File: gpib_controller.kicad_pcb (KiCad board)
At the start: 4 copper layers, 58.6 x 64.6 mm, 43 parts, among them J1 112-024-113R001, J2 FTSH-105-01-L-DV-K, J3 RJHSE5380, J4 USB4085-GF-A, U1 SN74LVC8T245PWR, U2 SN74LVC07APWR, U3 STM32H533RETx, U4 PTS645SH43SMTR92 LFS, U5 THVD1451D, U6 SN74LVC1G07DCKR, U7 SN74LVC14APWR, U8 USBLC6-2SC6, U9 TPSM861253RDXR, Y1 MU00525-32.768K, Y2 CS10820-24M

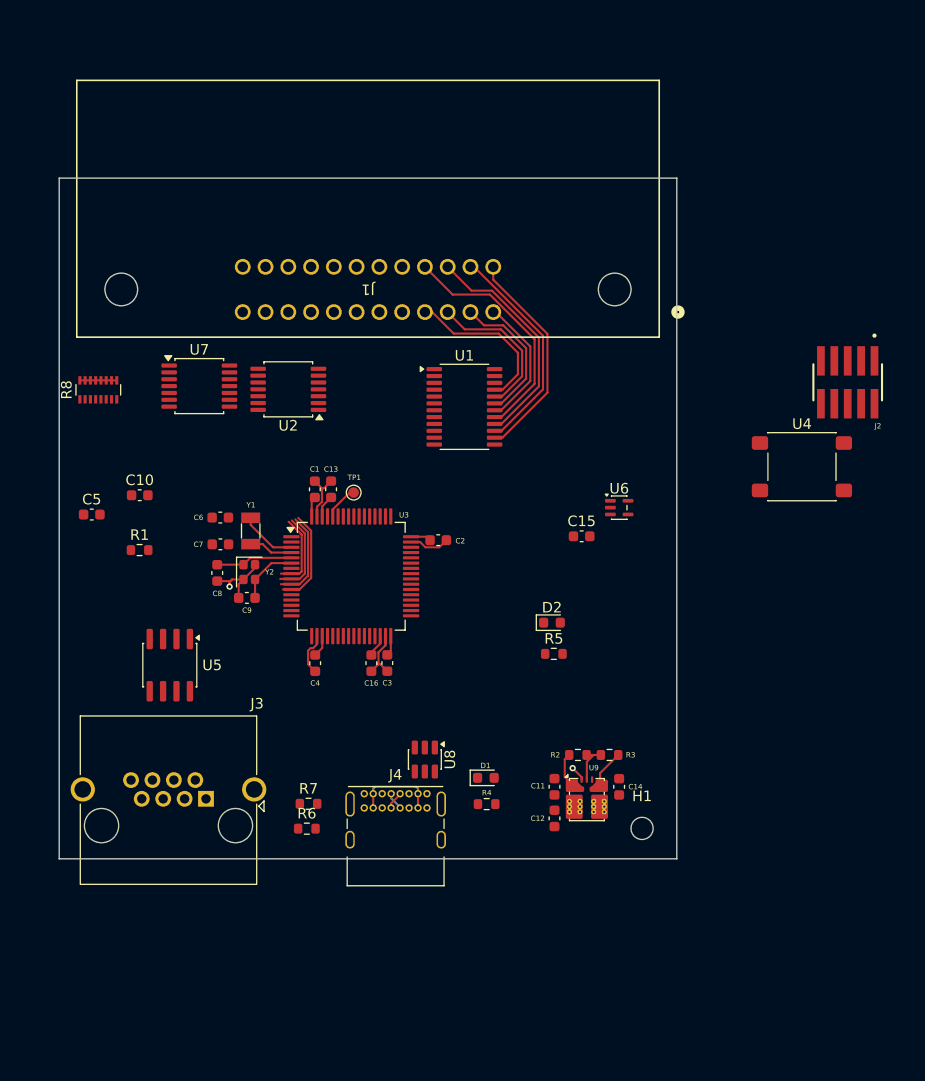
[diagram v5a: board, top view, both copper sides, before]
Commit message: Change board size, complete bottom routing, update (still broken) jobfile
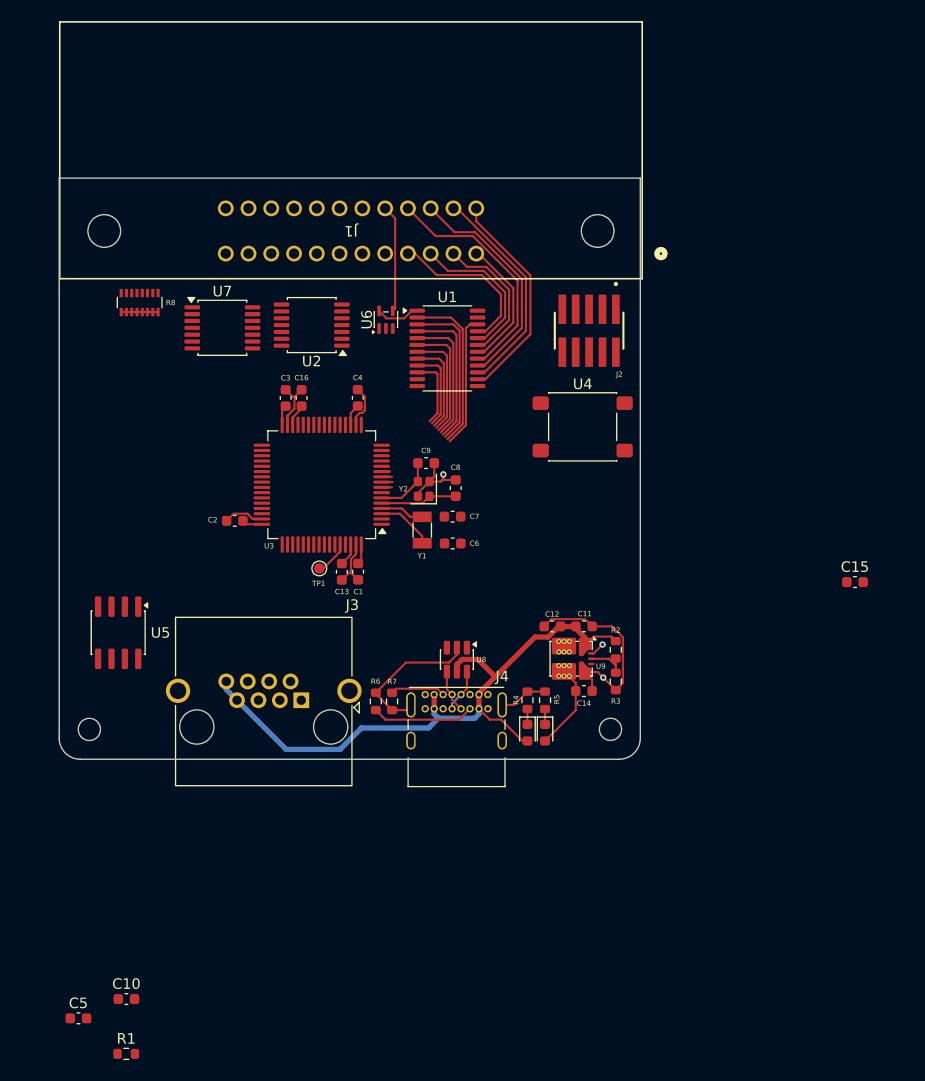
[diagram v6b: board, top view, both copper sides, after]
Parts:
- added H2: MountingHole, MountingHole:MountingHole_2.1mm, F.Cu at (189.4, 120.9)
- moved H1 53.3 mm to (140.0, 120.9)
- moved R1 47.8 mm to (143.4, 151.7)
- moved C5 47.8 mm to (138.9, 148.3)
- moved C10 47.8 mm to (143.5, 146.4)
- moved U6 28.4 mm to (168.1, 82.0), turned to 90 degrees
- moved C3 26.9 mm to (158.6, 89.4), turned to 90 degrees
- moved C15 26.3 mm to (212.6, 106.9)
- moved C16 26.0 mm to (160.1, 89.4), turned to 90 degrees
- moved C4 25.5 mm to (165.4, 89.4), turned to 90 degrees
- moved J2 25.0 mm to (187.3, 83.1)
- moved C8 24.0 mm to (174.7, 98.0), turned to -90 degrees
- moved C6 22.2 mm to (174.4, 103.2), turned to 180 degrees
- moved C7 22.2 mm to (174.4, 100.7), turned to 180 degrees
- moved C9 21.3 mm to (171.9, 95.6), turned to 180 degrees
- moved U4 21.1 mm to (186.7, 92.2)
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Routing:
- net +5V: track 15.0 -> 64.7 mm
- net GND: track 28.7 -> 63.3 mm, vias 1 -> 2
- net /Overview/GPIB Transceiver/GPIB_DIR: track 0.00 -> 15.8 mm
- net /Overview/GPIB Transceiver/GPIB_EN: track 0.00 -> 12.6 mm
- net +3V3: track 9.28 -> 21.8 mm
- net /Overview/GPIB Transceiver/iDIO8: track 0.00 -> 10.3 mm
- net /Overview/Connectors/REN: track 0.00 -> 10.2 mm
- net Net-(J4-CC2): track 0.00 -> 9.74 mm
- net /Overview/GPIB Transceiver/iDIO7: track 0.00 -> 9.02 mm
- net /Overview/GPIB Transceiver/iDIO6: track 0.00 -> 7.93 mm
- net /Overview/GPIB Transceiver/iDIO5: track 0.00 -> 6.79 mm
- net /Overview/GPIB Transceiver/iDIO4: track 9.33 -> 15.7 mm
- net /Overview/GPIB Transceiver/iDIO3: track 8.76 -> 14.9 mm
- net /Overview/GPIB Transceiver/iDIO2: track 8.11 -> 13.7 mm
- net Net-(J4-CC1): track 0.00 -> 5.23 mm
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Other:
- board size 58.6 x 64.6 mm -> 55.1 x 55.1 mm
- board text added: "3V3"
- board text added: "5V"

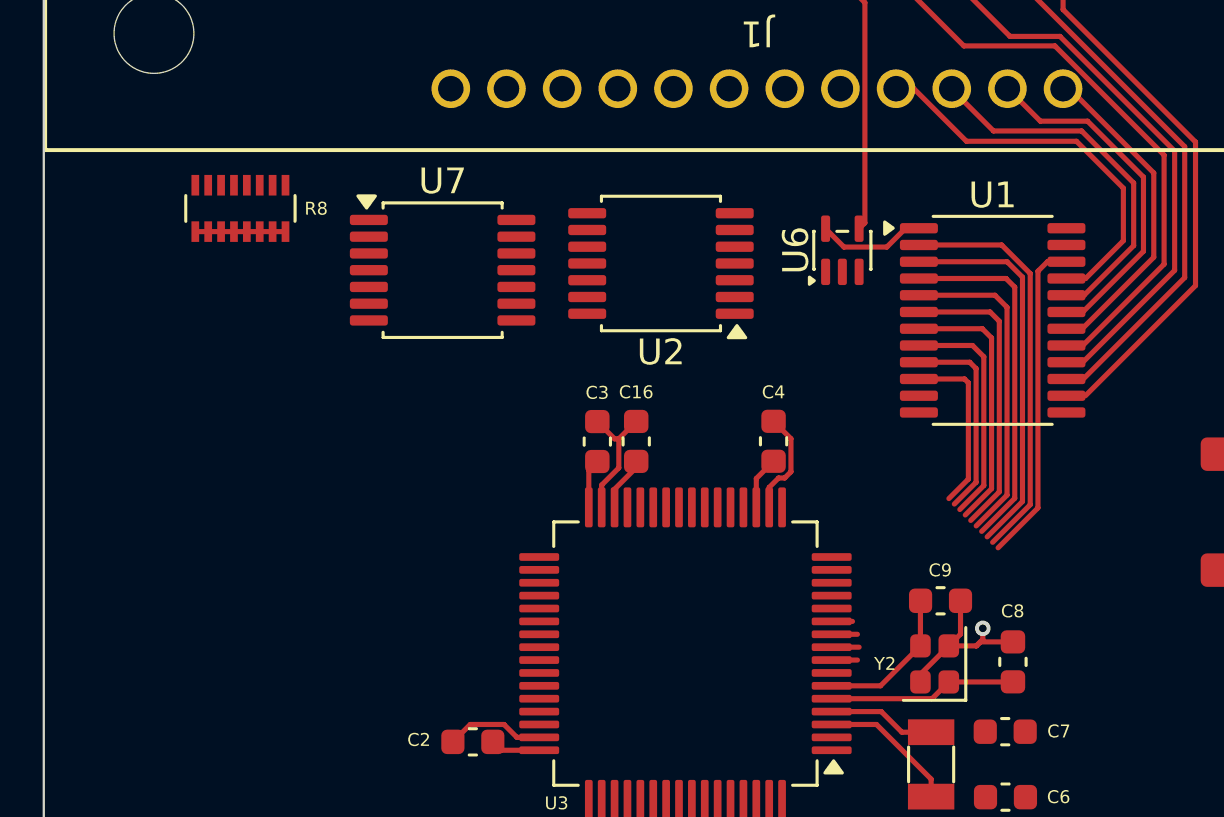
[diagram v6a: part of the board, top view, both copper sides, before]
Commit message: Update microcontroller pinouts and finished routing of DIO1-4
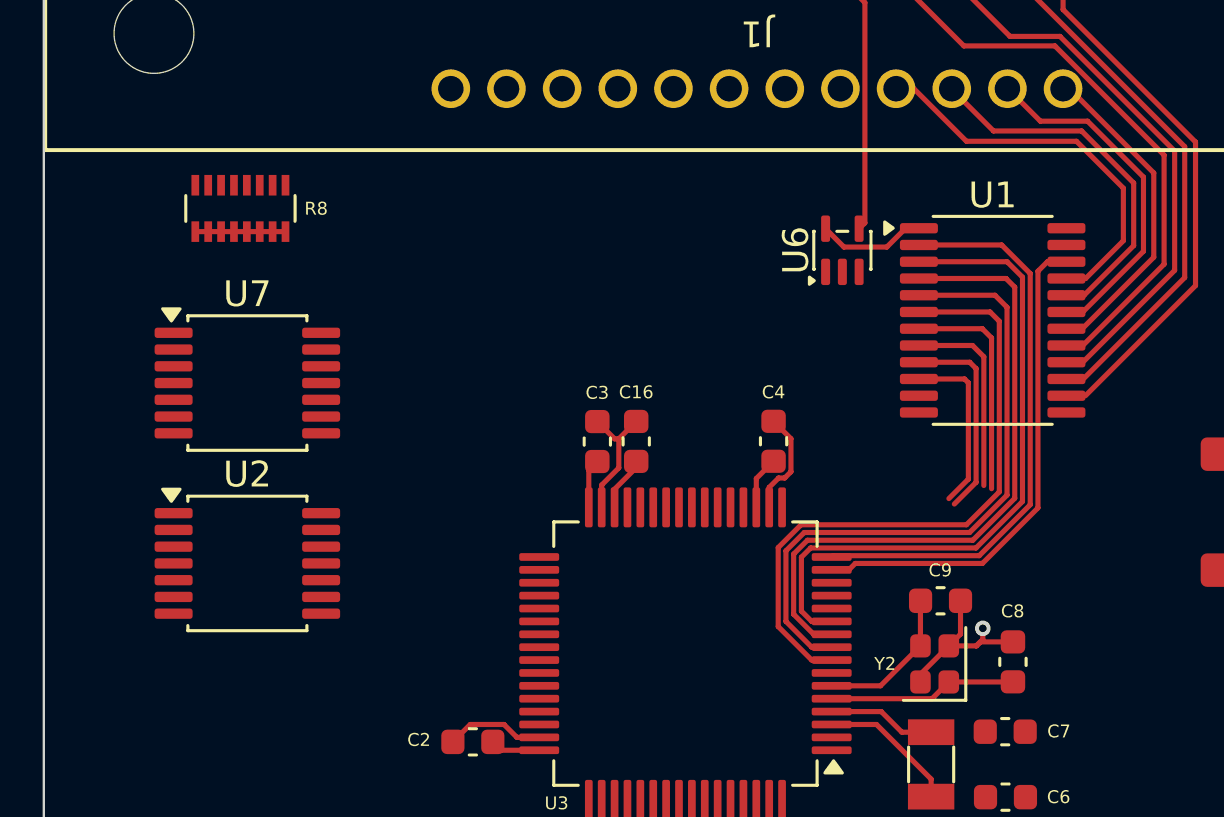
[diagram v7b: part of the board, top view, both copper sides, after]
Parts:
- moved U2 19.8 mm to (145.0, 94.2), turned to 0 degrees
- moved U7 8.75 mm to (145.0, 87.2)
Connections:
- U3 pad 15: /Overview/GPIB Transceiver/iDAV -> /Overview/GPIB Transceiver/GPIB_EN
- U3 pad 16: unconnected-(U3E-PA2(USART2_TX)-Pad16) -> /Overview/GPIB Transceiver/GPIB_DIR
- U3 pad 27: unconnected-(U3H-PB1-Pad27) -> /Overview/GPIB Transceiver/iDAV
- U3 pad 39: /Overview/GPIB Transceiver/GPIB_EN -> unconnected-(U3H-PC8-Pad39)
- U3 pad 40: /Overview/GPIB Transceiver/GPIB_DIR -> unconnected-(U3H-PC9-Pad40)
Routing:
- net /Overview/GPIB Transceiver/iDIO1: track 12.5 -> 25.0 mm
- net /Overview/GPIB Transceiver/iDIO2: track 13.7 -> 25.3 mm
- net /Overview/GPIB Transceiver/iDIO3: track 14.9 -> 25.7 mm
- net /Overview/GPIB Transceiver/iDIO4: track 15.7 -> 25.9 mm
- net /Overview/GPIB Transceiver/GPIB_EN: track 12.6 -> 19.4 mm
- net /Overview/GPIB Transceiver/GPIB_DIR: track 15.8 -> 22.3 mm
- net /Overview/GPIB Transceiver/iDIO8: track 10.3 -> 8.82 mm
- net /Overview/GPIB Transceiver/iDIO7: track 9.02 -> 7.70 mm

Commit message: Routing progress
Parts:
- moved C5 50.8 mm to (167.0, 105.9), turned to -90 degrees
- moved R1 47.1 mm to (161.7, 108.2)
- moved U4 44.3 mm to (143.6, 102.3), turned to -90 degrees
- moved J2 41.3 mm to (152.7, 105.7)
- moved C10 41.1 mm to (148.5, 105.7), turned to 90 degrees
- moved C15 23.1 mm to (190.7, 114.4), turned to 90 degrees
- moved U2 19.4 mm to (160.9, 83.0)
- moved U7 7.87 mm to (151.7, 83.0)
- moved C16 1.28 mm to (158.8, 89.4)
- moved C3 1.28 mm to (157.3, 89.4)
- moved U5 1.25 mm to (143.5, 112.7)
- moved C11 0.69 mm to (186.2, 111.0)
- moved C12 0.69 mm to (183.2, 111.0)
- moved C14 0.69 mm to (186.2, 117.2)
- moved R2 0.69 mm to (189.2, 113.3)
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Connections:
- R8 pad 1: /Overview/Connectors/DAV -> /Overview/Connectors/ATN
- R8 pad 2: /Overview/Connectors/NRFD -> /Overview/Connectors/SRQ
- R8 pad 3: /Overview/Connectors/NDAC -> /Overview/Connectors/IFC
- R8 pad 4: /Overview/Connectors/ATN -> /Overview/Connectors/NDAC
- R8 pad 5: /Overview/Connectors/IFC -> /Overview/Connectors/NRFD
- R8 pad 6: /Overview/Connectors/EOI -> /Overview/Connectors/DAV
- R8 pad 7: /Overview/Connectors/REN -> /Overview/Connectors/EOI
- R8 pad 8: /Overview/Connectors/SRQ -> /Overview/Connectors/REN
- U2 pad 1: /Overview/GPIB Transceiver/iDAV -> /Overview/GPIB Transceiver/iNDAC
- U2 pad 10: /Overview/Connectors/IFC -> /Overview/Connectors/DAV
- U2 pad 11: /Overview/GPIB Transceiver/iIFC -> /Overview/GPIB Transceiver/iDAV
- U2 pad 12: /Overview/Connectors/EOI -> /Overview/Connectors/NRFD
- U2 pad 13: /Overview/GPIB Transceiver/iEOI -> /Overview/GPIB Transceiver/iNRFD
- U2 pad 2: /Overview/Connectors/DAV -> /Overview/Connectors/NDAC
- U2 pad 3: /Overview/GPIB Transceiver/iNRFD -> /Overview/GPIB Transceiver/iIFC
- U2 pad 4: /Overview/Connectors/NRFD -> /Overview/Connectors/IFC
- U2 pad 5: /Overview/GPIB Transceiver/iNDAC -> /Overview/GPIB Transceiver/iATN
- U2 pad 6: /Overview/Connectors/NDAC -> /Overview/Connectors/ATN
- U2 pad 8: /Overview/Connectors/ATN -> /Overview/Connectors/EOI
- U2 pad 9: /Overview/GPIB Transceiver/iATN -> /Overview/GPIB Transceiver/iEOI
- U3 pad 20: /Overview/GPIB Transceiver/iNRFD -> /Overview/GPIB Transceiver/SRQ_SENSE
- U3 pad 27: /Overview/GPIB Transceiver/iDAV -> /Overview/GPIB Transceiver/iEOI
- U3 pad 28: unconnected-(U3H-PB2-Pad28) -> /Overview/GPIB Transceiver/iDAV
- U3 pad 29: /Overview/GPIB Transceiver/EOI_SENSE -> /Overview/GPIB Transceiver/iNRFD
- U3 pad 33: /Overview/GPIB Transceiver/SRQ_SENSE -> /Overview/GPIB Transceiver/iNDAC
- U3 pad 34: unconnected-(U3D-PB13(FDCAN2_TX)-Pad34) -> /Overview/GPIB Transceiver/iIFC
- U3 pad 39: unconnected-(U3H-PC8-Pad39) -> /Overview/GPIB Transceiver/iATN
- U3 pad 41: /Overview/GPIB Transceiver/iNDAC -> unconnected-(U3H-PA8-Pad41)
- U3 pad 42: /Overview/GPIB Transceiver/iATN -> unconnected-(U3H-PA9-Pad42)
- U3 pad 43: /Overview/GPIB Transceiver/iIFC -> unconnected-(U3H-PA10-Pad43)
- U3 pad 50: /Overview/GPIB Transceiver/iEOI -> /Overview/GPIB Transceiver/EOI_SENSE
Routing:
- net /Overview/Connectors/EOI: track 0.00 -> 40.1 mm
- net /Overview/Connectors/DAV: track 0.00 -> 35.0 mm
- net /Overview/Connectors/NRFD: track 0.00 -> 31.3 mm
- net /Overview/Connectors/NDAC: track 0.00 -> 28.9 mm
- net /Overview/Connectors/REN: track 10.2 -> 38.9 mm
- net GND: track 63.3 -> 91.6 mm, vias 2 -> 3
- net /Overview/Connectors/IFC: track 0.00 -> 26.4 mm
- net /Overview/Connectors/CTRL_TX_N: track 0.00 -> 23.4 mm
- net /Overview/Connectors/ATN: track 0.00 -> 21.5 mm
- net /Overview/GPIB Transceiver/iATN: track 0.00 -> 18.5 mm
- net /Overview/Connectors/CTRL_RX_N: track 0.00 -> 18.5 mm
- net /Overview/GPIB Transceiver/iNDAC: track 0.00 -> 18.5 mm
- net /Overview/GPIB Transceiver/iDIO8: track 8.82 -> 26.5 mm, vias 0 -> 2
- net /Overview/GPIB Transceiver/iIFC: track 0.00 -> 17.7 mm
- net /Overview/GPIB Transceiver/iDIO7: track 7.70 -> 24.5 mm, vias 0 -> 2
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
